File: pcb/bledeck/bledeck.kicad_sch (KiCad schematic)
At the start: 35 parts, among them J1 Conn_01x09_Socket, J2 Conn_01x02_Socket, U1 ESP32-DEVKIT-V1

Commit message: generate gerber, fix pin number
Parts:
- J2: footprint (none) -> Connector_PinHeader_2.54mm:PinHeader_1x02_P2.54mm_Vertical
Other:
- company: (none) -> Davide "Argaar" Foschi
- title: (none) -> BLEDeck
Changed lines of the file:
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@@
 	(generator_version "9.0")
 	(paper "A4")
+	(title_block
+		(title "BLEDeck")
+		(date "2025-11-11")
+		(rev "1.0")
+		(company "Davide \"Argaar\" Foschi")
+	)
 	(junction
 		(at 189.23 57.15)
@@
 			)
 		)
-		(property "Footprint" ""
+		(property "Footprint" "Connector_PinHeader_2.54mm:PinHeader_1x02_P2.54mm_Vertical"
 			(at 109.22 49.53 0)
 			(effects

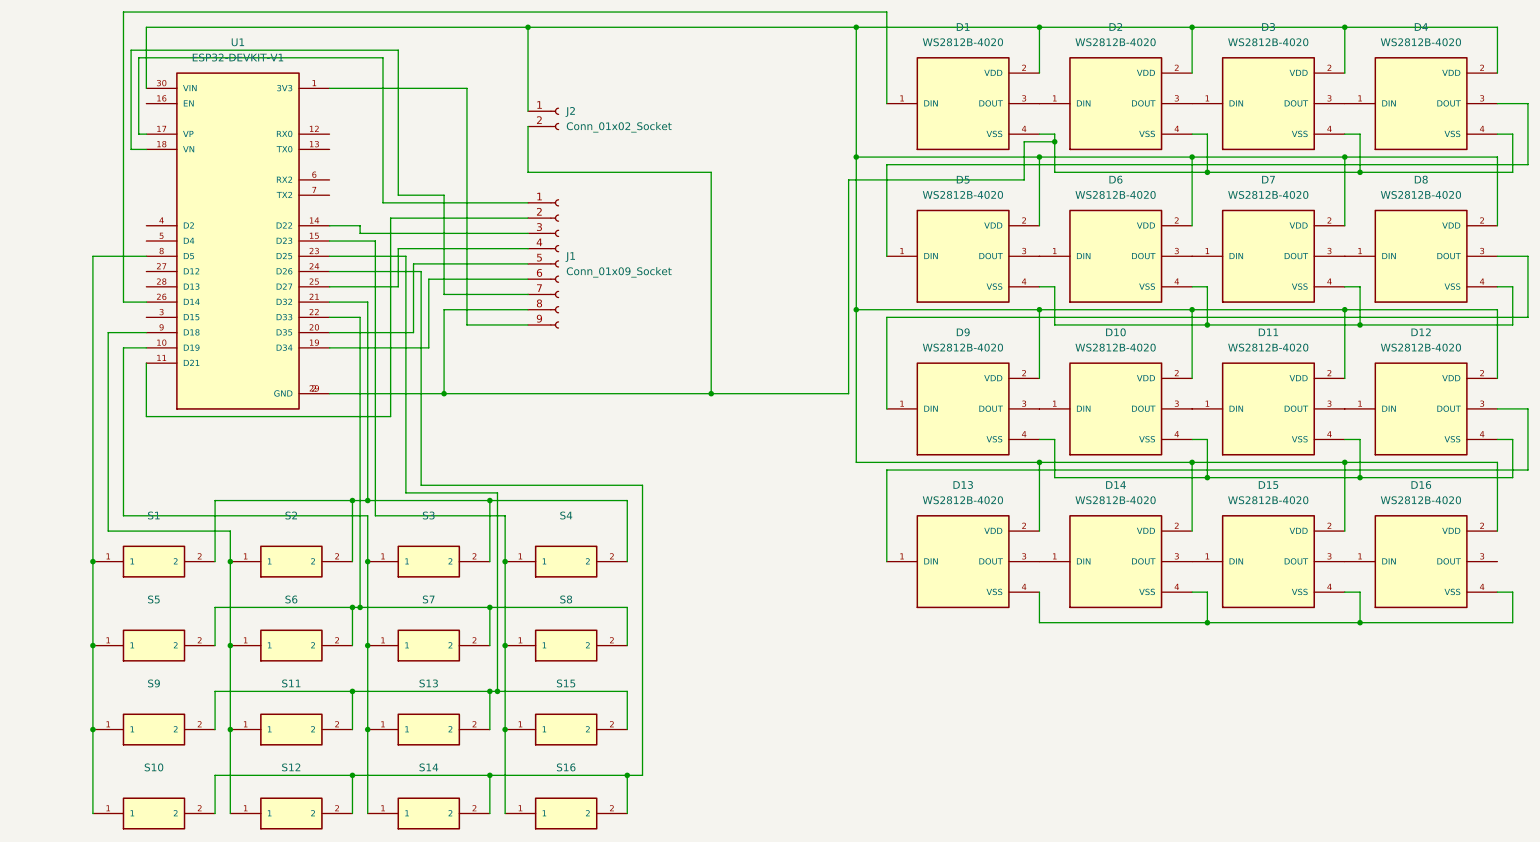
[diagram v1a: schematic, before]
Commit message: pcb add libraries and readme with licenses
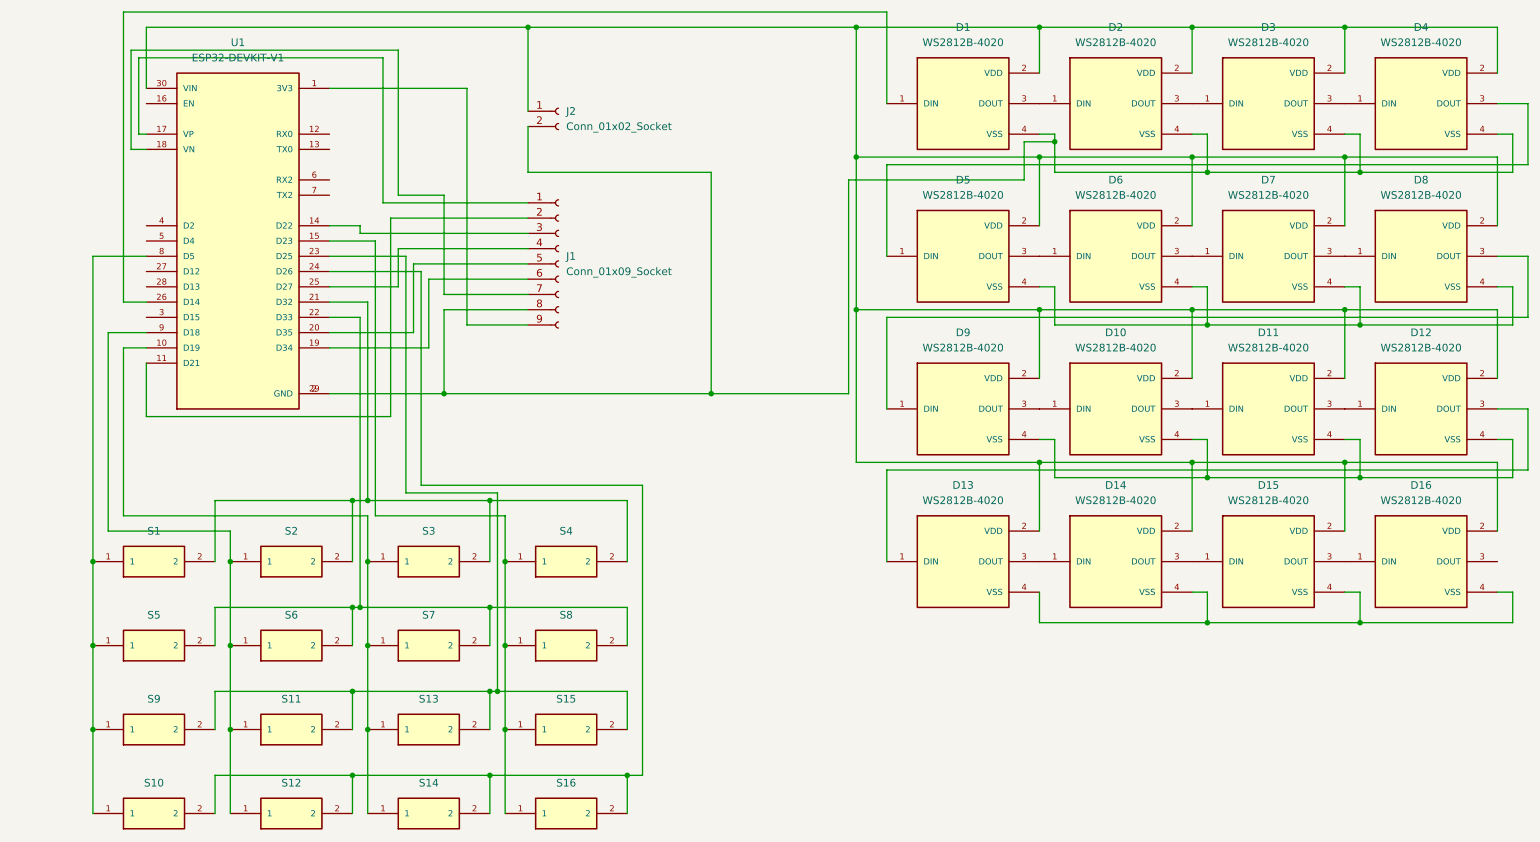
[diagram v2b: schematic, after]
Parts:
- D1, D10, D11, D12, D13, D14, D15, D16, D2, D3, D4, D5, D6, D7, D8, D9: symbol Device:WS2812B-4020 -> BLEDeck:WS2812B-4020
- J2: footprint Connector_PinHeader_2.54mm:PinHeader_1x02_P2.54mm_Vertical -> BLEDeck:PinHeader_1x02_P2.54mm_Vertical
- S1, S10, S11, S12, S13, S14, S15, S16, S2, S3, S4, S5, S6, S7, S8, S9: footprint Connector:Kailh_socket_MX -> PG151101S11:SW_PG151101S11; symbol PG151101S11:PG151101S11 -> BLEDeck:PG151101S11
- U1: footprint BLEDeck:MODULE_ESP32_DEVKIT_V1 -> ESP32-DEVKIT-V1:MODULE_ESP32_DEVKIT_V1; symbol Esp32:ESP32-DEVKIT-V1 -> BLEDeck:ESP32-DEVKIT-V1

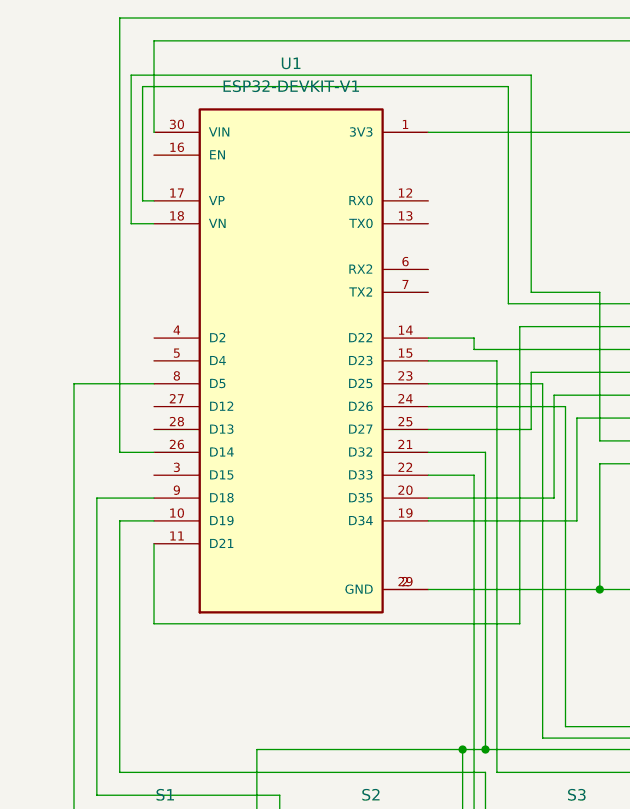
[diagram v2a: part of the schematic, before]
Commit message: [firmware] add battery info [pcb] evenly spaced keys, fix oled pins position, reroute all tracks/vias, add gerber zip for jlcpcb
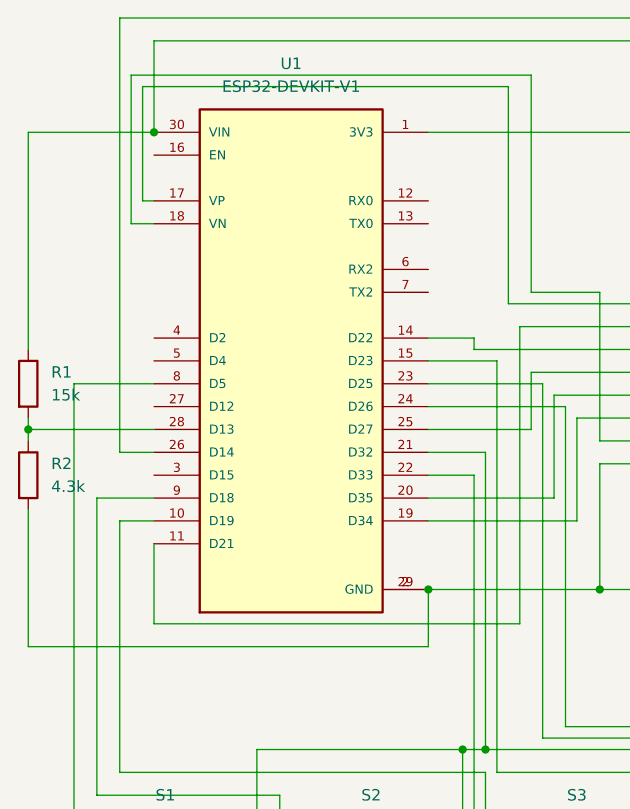
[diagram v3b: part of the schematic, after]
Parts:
- added R1: 15k, Resistor_THT:R_Axial_DIN0207_L6.3mm_D2.5mm_P7.62mm_Horizontal, symbol Device:R
- added R2: 4.3k, Resistor_THT:R_Axial_DIN0207_L6.3mm_D2.5mm_P7.62mm_Horizontal, symbol Device:R
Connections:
- net at D1.2 (VDD), D10.2 (VDD), D11.2 (VDD)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: now also R1.1
- net at D1.4 (VSS), D2.4 (VSS), D3.4 (VSS)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: now also R2.2
- net at U1.28 (D13): now also R1.2, R2.1
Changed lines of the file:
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@@
 	)
 	(junction
+		(at 40.64 45.72)
+		(diameter 0)
+		(color 0 0 0 0)
+	)
+	(junction
+		(at 26.67 78.74)
+		(diameter 0)
+		(color 0 0 0 0)
+	)
+	(junction
 		(at 74.93 146.05)
 		(diameter 0)
@@
 	)
 	(junction
+		(at 71.12 96.52)
+		(diameter 0)
+		(color 0 0 0 0)
+	)
+	(junction
 		(at 240.03 82.55)
 		(diameter 0)
@@
 	(wire
 		(pts
+			(xy 26.67 78.74) (xy 40.64 78.74)
+		)
+		(stroke
+			(width 0)
+			(type default)
+		)
+	)
+	(wire
+		(pts
 			(xy 52.07 166.37) (xy 52.07 160.02)
 		)
@@
 	(wire
 		(pts
+			(xy 40.64 45.72) (xy 26.67 45.72)
+		)
+		(stroke
+			(width 0)
+			(type default)
+		)
+	)
+	(wire
+		(pts
 			(xy 189.23 107.95) (xy 214.63 107.95)
 		)
@@
 	(wire
 		(pts
+			(xy 26.67 45.72) (xy 26.67 69.85)
+		)
+		(stroke
+			(width 0)
+			(type default)
+		)
+	)
+	(wire
+		(pts
 			(xy 31.75 73.66) (xy 31.75 124.46)
 		)
@@
 	(wire
 		(pts
+			(xy 71.12 102.87) (xy 26.67 102.87)
+		)
+		(stroke
+			(width 0)
+			(type default)
+		)
+	)
+	(wire
+		(pts
 			(xy 77.47 81.28) (xy 77.47 114.3)
 		)
@@
 	(wire
 		(pts
+			(xy 71.12 96.52) (xy 71.12 102.87)
+		)
+		(stroke
+			(width 0)
+			(type default)
+		)
+	)
+	(wire
+		(pts
 			(xy 104.14 72.39) (xy 82.55 72.39)
 		)
@@
 	(wire
 		(pts
+			(xy 26.67 80.01) (xy 26.67 78.74)
+		)
+		(stroke
+			(width 0)
+			(type default)
+		)
+	)
+	(wire
+		(pts
 			(xy 104.14 67.31) (xy 81.28 67.31)
 		)
@@
 	(wire
 		(pts
+			(xy 26.67 77.47) (xy 26.67 78.74)
+		)
+		(stroke
+			(width 0)
+			(type default)
+		)
+	)
+	(wire
+		(pts
 			(xy 36.83 88.9) (xy 36.83 116.84)
 		)
@@
 	(wire
 		(pts
+			(xy 26.67 102.87) (xy 26.67 87.63)
+		)
+		(stroke
+			(width 0)
+			(type default)
+		)
+	)
+	(wire
+		(pts
 			(xy 265.43 129.54) (xy 267.97 129.54)
 		)
@@
 	)
 	(symbol
+		(lib_id "Device:R")
+		(at 26.67 73.66 0)
+		(unit 1)
+		(exclude_from_sim no)
+		(in_bom yes)
+		(on_board yes)
+		(dnp no)
+		(fields_autoplaced yes)
+		(property "Reference" "R1"
+			(at 29.21 72.3899 0)
+			(effects
+				(font
+					(size 1.27 1.27)
+				)
+				(justify left)
+			)
+		)
+		(property "Value" "15k"
+			(at 29.21 74.9299 0)
+			(effects
+				(font
+					(size 1.27 1.27)
+				)
+				(justify left)
+			)
+		)
+		(property "Footprint" "Resistor_THT:R_Axial_DIN0207_L6.3mm_D2.5mm_P7.62mm_Horizontal"
+			(at 24.892 73.66 90)
+			(effects
+				(font
+					(size 1.27 1.27)
+				)
+				(hide yes)
+			)
+		)
+		(property "Datasheet" "~"
+			(at 26.67 73.66 0)
+			(effects
+				(font
+					(size 1.27 1.27)
+				)
+				(hide yes)
+			)
+		)
+		(property "Description" "Resistor"
+			(at 26.67 73.66 0)
+			(effects
+				(font
+					(size 1.27 1.27)
+				)
+				(hide yes)
+			)
+		)
+		(pin "2"
+		)
+		(pin "1"
+		)
+		(instances
+			(project ""
+				(path "/8bba6075-8a84-4835-a7b9-00f9c9f191ba"
+					(reference "R1")
+					(unit 1)
+				)
+			)
+		)
+	)
+	(symbol
 		(lib_id "BLEDeck:PG151101S11")
 		(at 87.63 138.43 0)
@@
 					(unit 1)
 				)
+			)
+		)
+	)
+	(symbol
+		(lib_id "Device:R")
+		(at 26.67 83.82 0)
+		(unit 1)
+		(exclude_from_sim no)
+		(in_bom yes)
+		(on_board yes)
+		(dnp no)
+		(fields_autoplaced yes)
+		(property "Reference" "R2"
+			(at 29.21 82.5499 0)
+			(effects
+				(font
+					(size 1.27 1.27)
+				)
+				(justify left)
+			)
+		)
+		(property "Value" "4.3k"
+			(at 29.21 85.0899 0)
+			(effects
+				(font
+					(size 1.27 1.27)
+				)
+				(justify left)
+			)
+		)
+		(property "Footprint" "Resistor_THT:R_Axial_DIN0207_L6.3mm_D2.5mm_P7.62mm_Horizontal"
+			(at 24.892 83.82 90)
+			(effects
+				(font
+					(size 1.27 1.27)
+				)
+				(hide yes)
+			)
+		)
+		(property "Datasheet" "~"
+			(at 26.67 83.82 0)
+			(effects
+				(font
+					(size 1.27 1.27)
+				)
+				(hide yes)
+			)
+		)
+		(property "Description" "Resistor"
+			(at 26.67 83.82 0)
+			(effects
+				(font
+					(size 1.27 1.27)
+				)
+				(hide yes)
+			)
+		)
+		(pin "2"
+		)
+		(pin "1"
+		)
+		(instances
+			(project "bledeck"
+				(path "/8bba6075-8a84-4835-a7b9-00f9c9f191ba"
+					(reference "R2")
+					(unit 1)
+				)
